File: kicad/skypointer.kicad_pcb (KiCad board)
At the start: 2 copper layers, 45.5 x 27.5 mm, 7 parts, among them P1 CONN_01X04, P3 Laser, U1 TCST1230

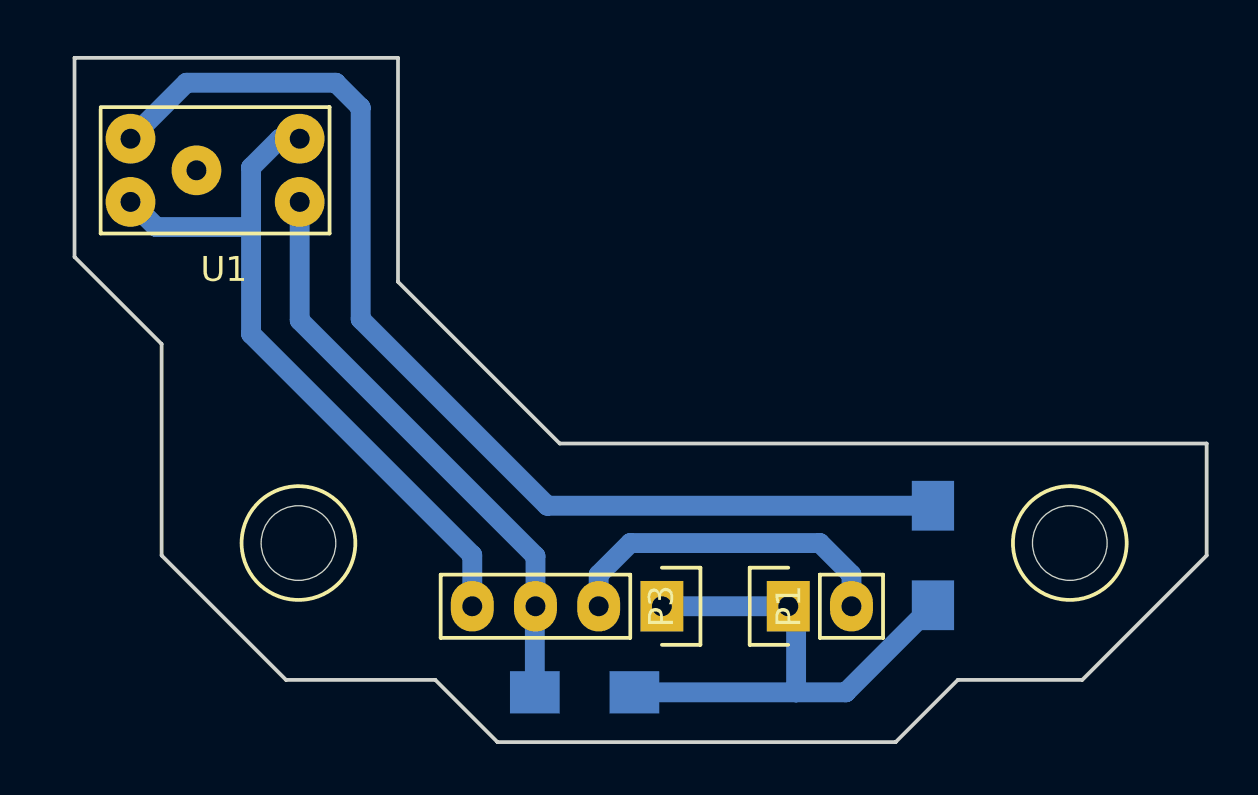
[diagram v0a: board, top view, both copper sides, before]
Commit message: Add a MOSFET to the PCB
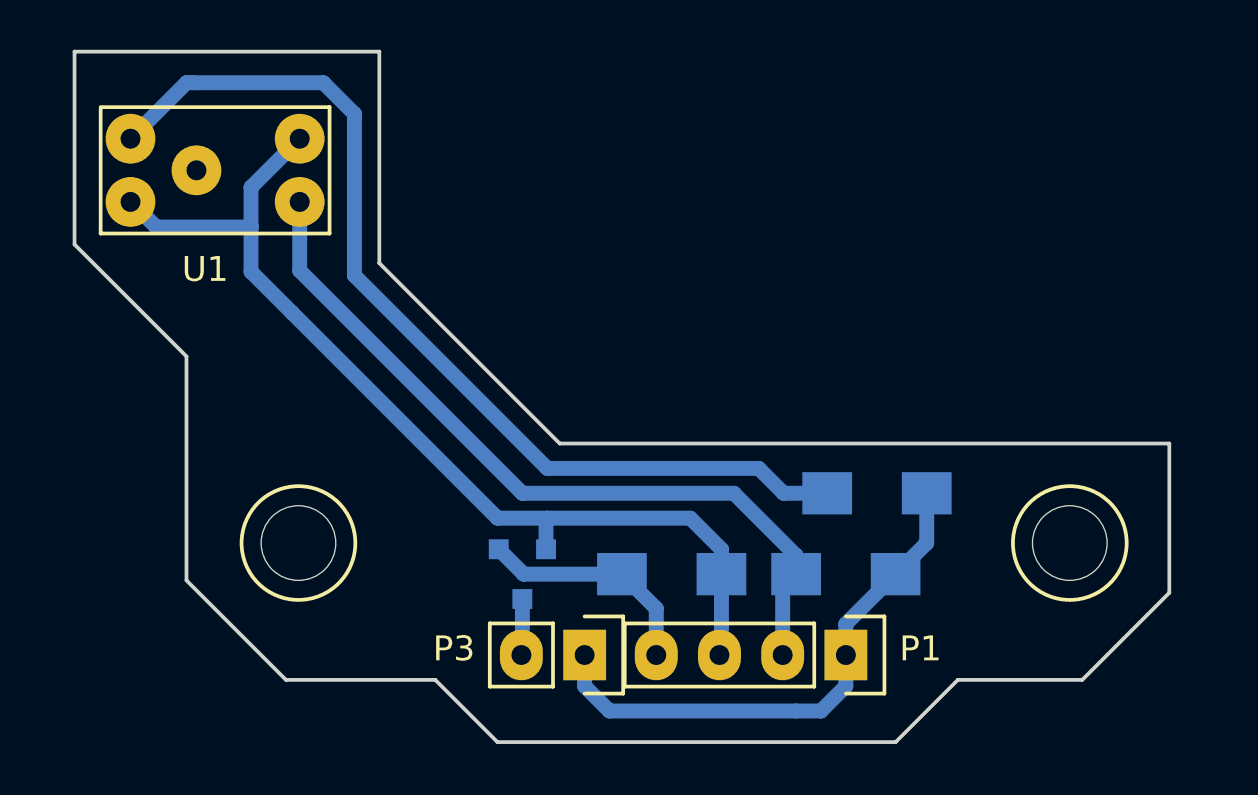
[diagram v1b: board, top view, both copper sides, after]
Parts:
- added Q1: SI2302DS, SOT-23, B.Cu at (121.0, 116.2)
- added R3: 100k, Resistors_SMD:R_1206_HandSoldering, B.Cu at (127.0, 116.2)
- moved R2 11.5 mm to (134.0, 116.2)
- moved P3 8.42 mm to (123.5, 119.5), turned to 270 degrees
- moved P1 7.65 mm to (134.0, 119.5)
- moved R1 3.36 mm to (135.2, 113.0), turned to 180 degrees
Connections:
- P1 pad 3: Net-(P1-Pad3) -> GND
- P1 pad 4: GND -> Net-(P1-Pad4)
- P3 pad 2: Net-(P1-Pad2) -> Net-(P3-Pad2)
- R2 pad 2: Net-(P1-Pad3) -> Net-(P1-Pad2)
- U1 pad 3: Net-(P1-Pad3) -> Net-(P1-Pad2)
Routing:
- net Net-(P1-Pad3): track 23.6 -> 0.00 mm
- net Net-(P1-Pad2): track 13.8 -> 31.7 mm
- net GND: track 29.0 -> 40.5 mm
- net Net-(P1-Pad4): track 0.00 -> 9.19 mm
- net Net-(R1-Pad2): track 45.2 -> 39.6 mm
- net Net-(P3-Pad2): track 0.00 -> 2.27 mm
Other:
- board size 45.5 x 27.5 mm -> 44 x 27.8 mm
- net class Default: trace_width 0.8 -> 0.6
- net class small added: clearance 0.2, trace_width 0.6, via_dia 1.2, via_drill 0.6

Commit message: Fix pcb dimensions
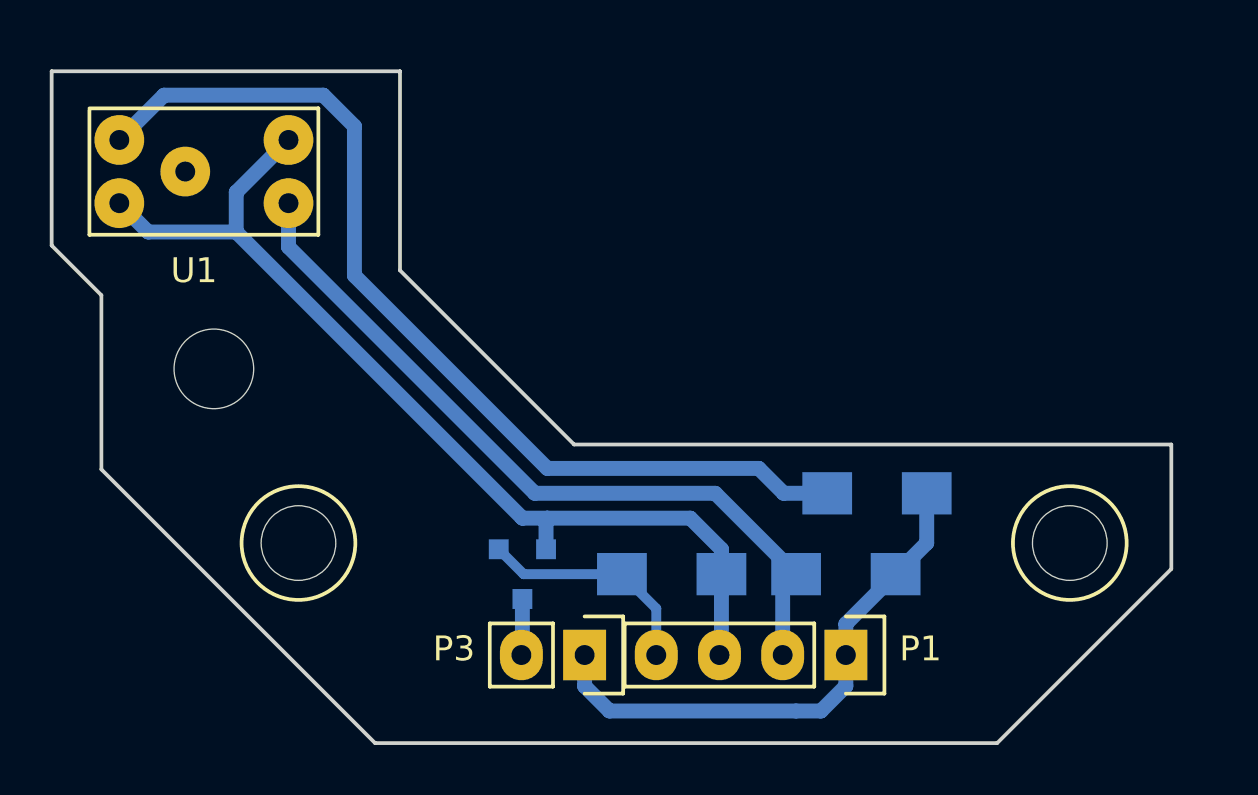
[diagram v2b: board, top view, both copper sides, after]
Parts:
- added REF**: MountingHole_3.2mm_M3, Mounting_Holes:MountingHole_3.2mm_M3, F.Cu at (108.6, 108.0)
- moved U1 0.45 mm to (104.8, 98.8)
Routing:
- net Net-(P1-Pad2): track 31.7 -> 31.1 mm
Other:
- board size 44 x 27.8 mm -> 45 x 27 mm
- net class Default: clearance 0.4 -> 0.3
- net class small: trace_width 0.6 -> 0.4
- rule trace_clearance: 0.4 -> 0.3

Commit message: Remove MOSFET from PCB
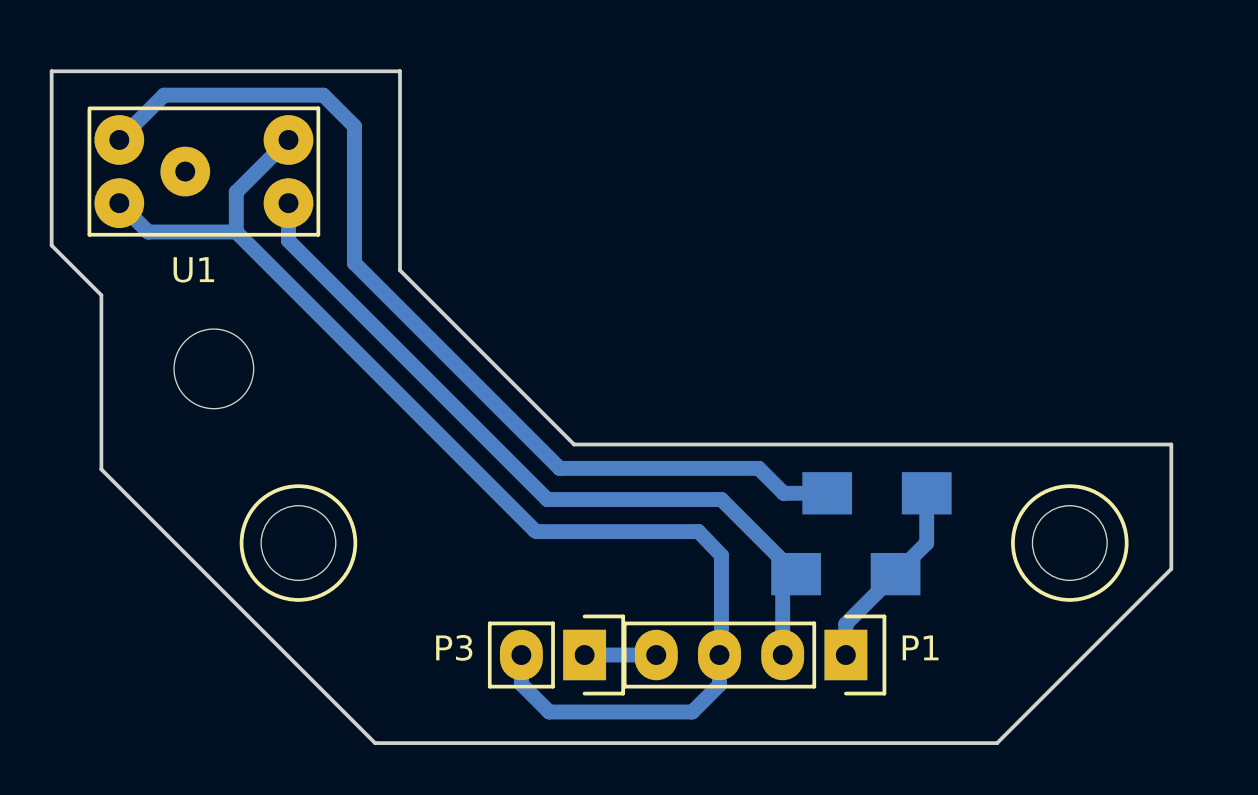
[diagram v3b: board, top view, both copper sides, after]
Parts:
- removed Q1: SI2302DS, SOT-23
- removed R3: 100k, Resistors_SMD:R_1206_HandSoldering
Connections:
- P3 pad 1: +5V -> Net-(P1-Pad4)
- P3 pad 2: Net-(P3-Pad2) -> GND
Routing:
- net +5V: track 21.7 -> 7.85 mm
- net GND: track 40.1 -> 49.8 mm
- net Net-(P1-Pad4): track 9.19 -> 2.88 mm
- net Net-(P3-Pad2): track 2.27 -> 0.00 mm
